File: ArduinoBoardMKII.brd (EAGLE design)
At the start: 95.2 x 82.5 mm, 22 parts

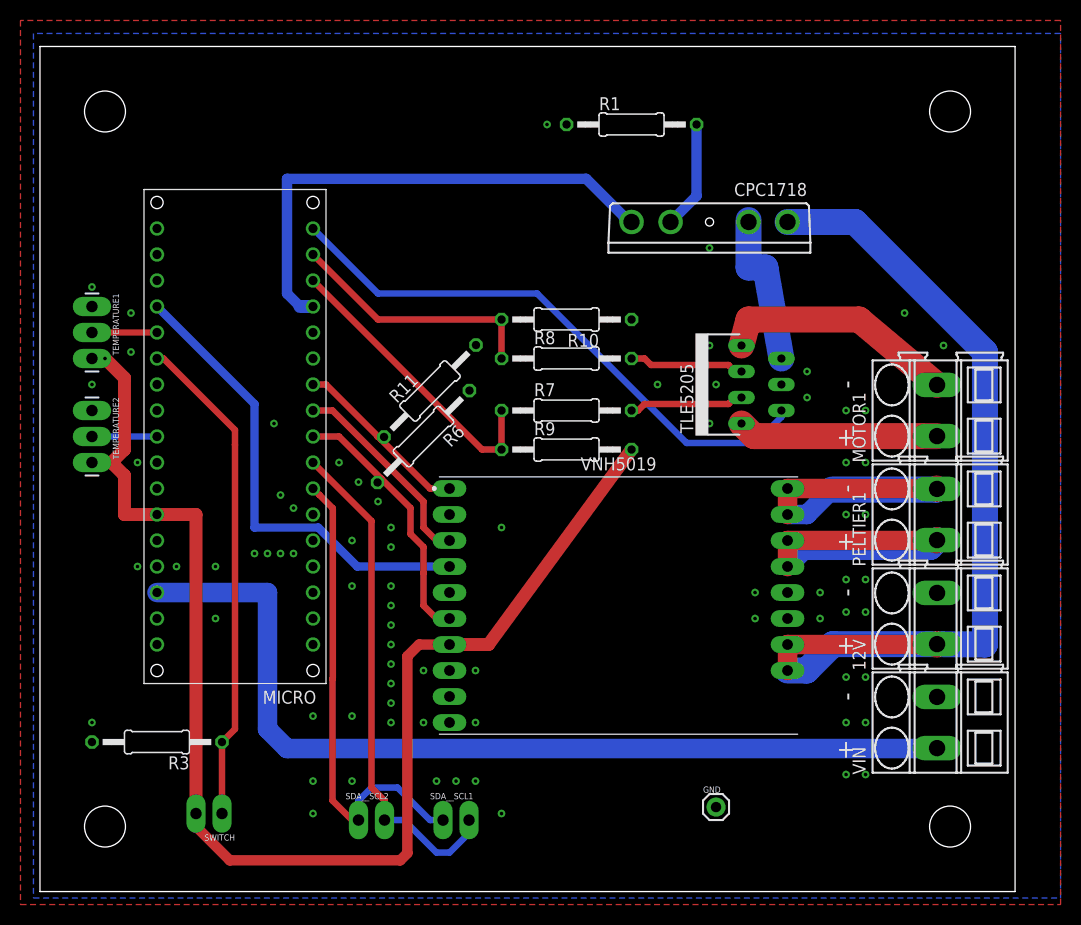
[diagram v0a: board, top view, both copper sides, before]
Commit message: Arduino Side Headers
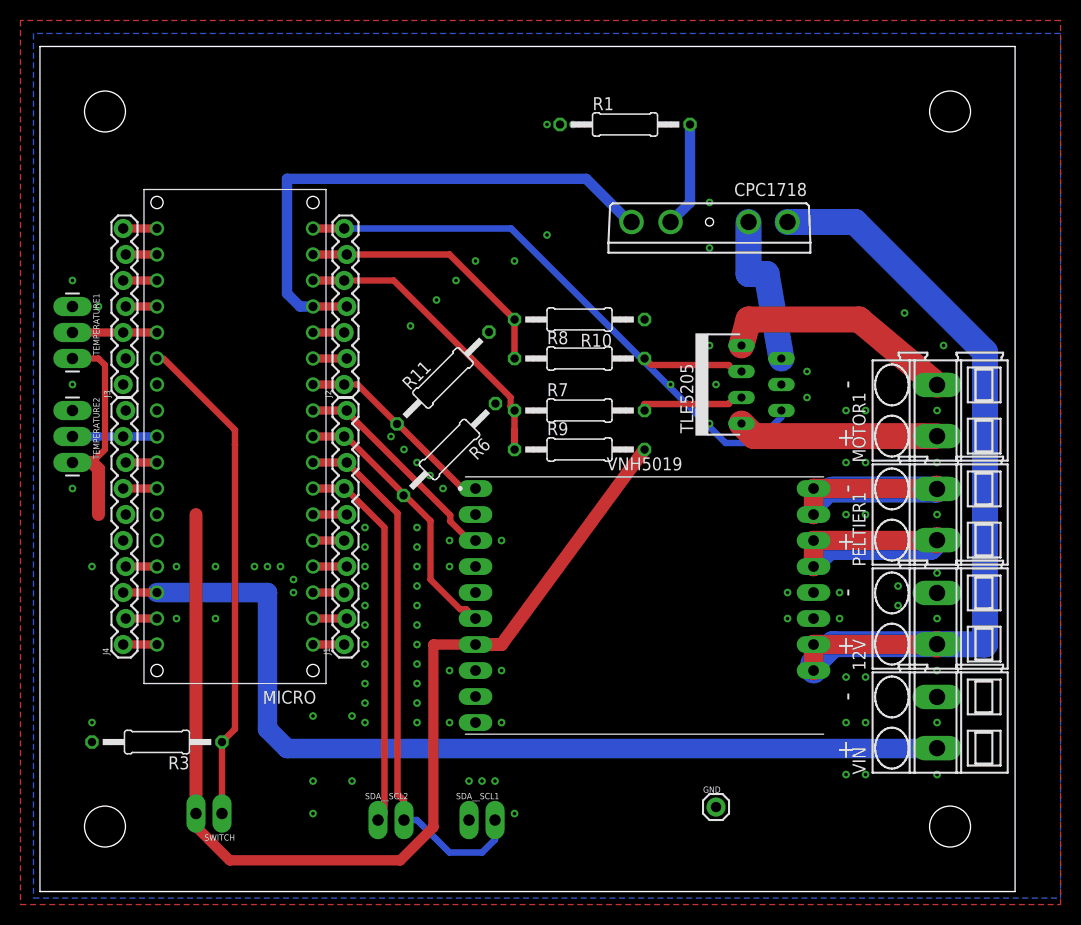
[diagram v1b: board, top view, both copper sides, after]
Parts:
- added J1, J4: (no value), SparkFun-Connectors:1X10_LOCK
- added J2, J3: (no value), SparkFun-Connectors:1X07_LOCK
- moved R6 2.84 mm to (40.0, 43.2)
- moved SDA__SCL1 2.54 mm to (41.9, 6.99)
- moved VNH5019 2.54 mm to (59.1, 27.9)
- moved SDA__SCL2 1.91 mm to (33.0, 6.99)
- moved TEMPERATURE1 1.91 mm to (3.17, 57.1)
- moved TEMPERATURE2 1.91 mm to (3.17, 47.0)
- moved R11 1.80 mm to (39.4, 50.2)
- moved R10 1.27 mm to (52.7, 55.9)
- moved R7 1.27 mm to (52.7, 47.0)
- moved R8 1.27 mm to (52.7, 52.1)
- moved R9 1.27 mm to (52.7, 43.2)
- moved R1 0.63 mm to (57.1, 74.9)
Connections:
- new net N$1: J4.4, MICRO.GND1
- new net N$10: J1.1, MICRO.MOSI
- new net N$11: J3.1, MICRO.A3
- new net N$12: J3.2, MICRO.A2
- new net N$14: J3.4, MICRO.A0
- new net N$15: J3.5, MICRO.REF
- new net N$16: J3.6, MICRO.3V3
- new net N$17: J3.7, MICRO.D13
- new net N$18: J4.10, MICRO.A4
- new net N$19: J4.5, MICRO.RST1
- new net N$2: J4.6, MICRO.5V
- new net N$20: J4.8, MICRO.NC8
- new net N$23: J4.7, MICRO.NC7
- new net N$25: J4.2, MICRO.MISO
- new net N$26: J4.1, MICRO.SCK
- new net N$5: J1.6, MICRO.GND
- new net N$6: J1.5, MICRO.RST
- new net N$7: J1.4, MICRO.RX
- new net N$8: J1.3, MICRO.TX
- new net N$9: J1.2, MICRO.SS
- net +5V: no longer MICRO.5V
- net DOORSWITCH: no longer MICRO.A2
- net GND: no longer MICRO.GND, MICRO.GND1
- net MOTOR-ENABLE: now also J2.4
- net MOTOR-ERRORFLAG: now also J2.7
- net MOTOR-IN1: now also J2.5
- net MOTOR-IN2: now also J2.6
- net N$21: now also J2.2
- net N$22: now also J2.3
- net PELTIER-CURRENT: no longer MICRO.A0
- net PELTIER-INA: now also J2.1
- net PELTIER-INB: now also J1.9
- net PELTIER-PWM: now also J1.10
- net SCL: now also J1.8
- net SDA: now also J1.7
- net TEMPERATURE1: now also J3.3
- net TEMPERATURE2: now also J4.9
- net VIN: now also J4.3
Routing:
- net PELTIER-CURRENT: track 46.2 -> 0.00 mm
- net SDA: track 46.6 -> 37.4 mm
- net +5V: track 131.3 -> 125.2 mm, vias 1 -> 0
- net PELTIER-OUTB: track 32.8 -> 27.8 mm
- net PELTIER-OUTA: track 32.8 -> 28.1 mm
- net +12V: track 90.6 -> 85.9 mm
- net SCL: track 49.4 -> 53.2 mm
- net MOTOR-ENABLE: track 49.7 -> 53.2 mm
- net VIN: track 90.3 -> 93.6 mm
- net N$9: track 0.00 -> 3.30 mm
- net N$7: track 0.00 -> 3.30 mm
- net N$5: track 0.00 -> 3.30 mm
- net N$26: track 0.00 -> 3.30 mm
- net N$23: track 0.00 -> 3.30 mm
- net N$21: track 0.00 -> 3.30 mm
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
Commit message: Electron Side Header Start
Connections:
- removed net N$12: J3.2, MICRO.A2
- removed net N$2: J4.6, MICRO.5V
- net +5V: now also J4.6, MICRO.5V
- net DOORSWITCH: now also J3.2, MICRO.A2
- net GND: now also GND.1
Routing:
- net +5V: track 125.2 -> 134.8 mm
- net DOORSWITCH: track 47.9 -> 51.9 mm
- net N$19: track 0.00 -> 3.30 mm
- net N$11: track 0.00 -> 3.30 mm
- net N$18: track 0.00 -> 3.05 mm
